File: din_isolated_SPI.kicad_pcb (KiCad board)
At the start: 2 copper layers, 31.8 x 40.5 mm, 19 parts, among them J1 CONN_01X10, U1 SI8661AB-B-IS1, U4 WeMos_mini

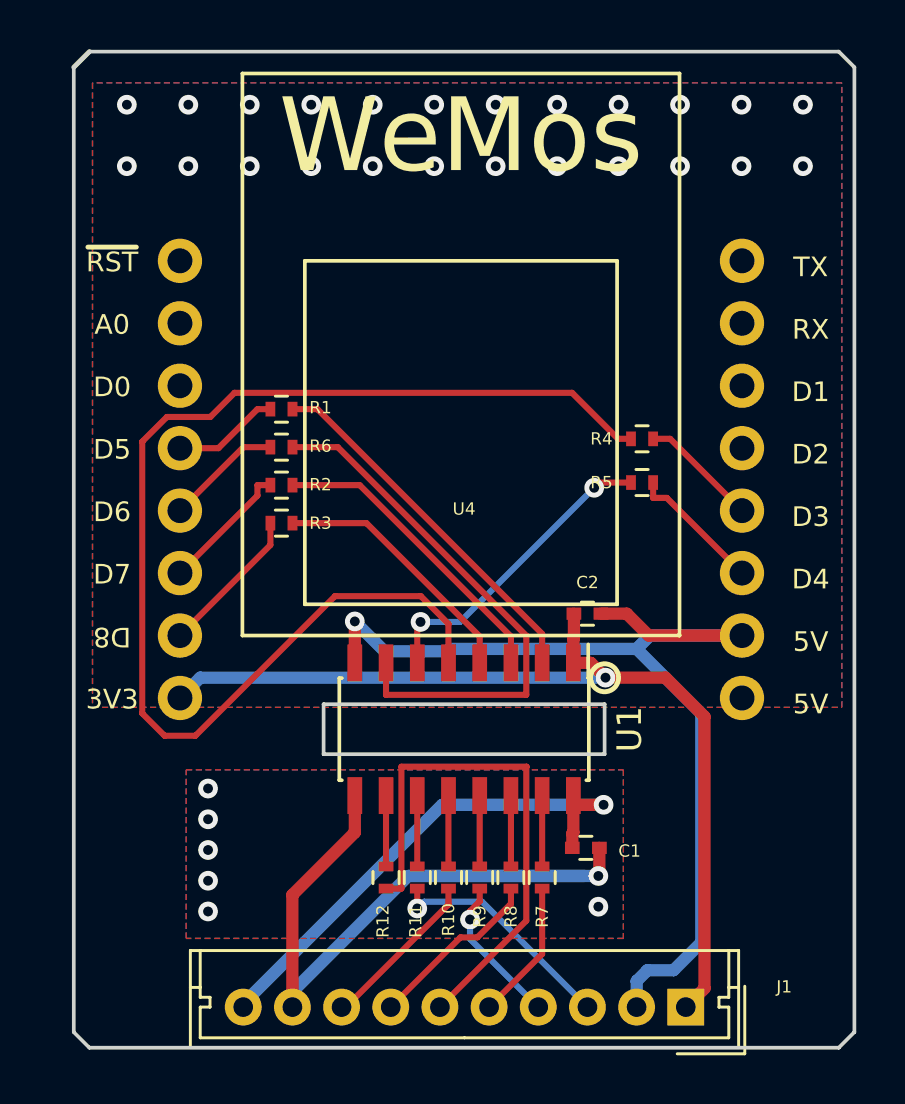
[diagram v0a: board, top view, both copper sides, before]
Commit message: Change to 0603 and reroute
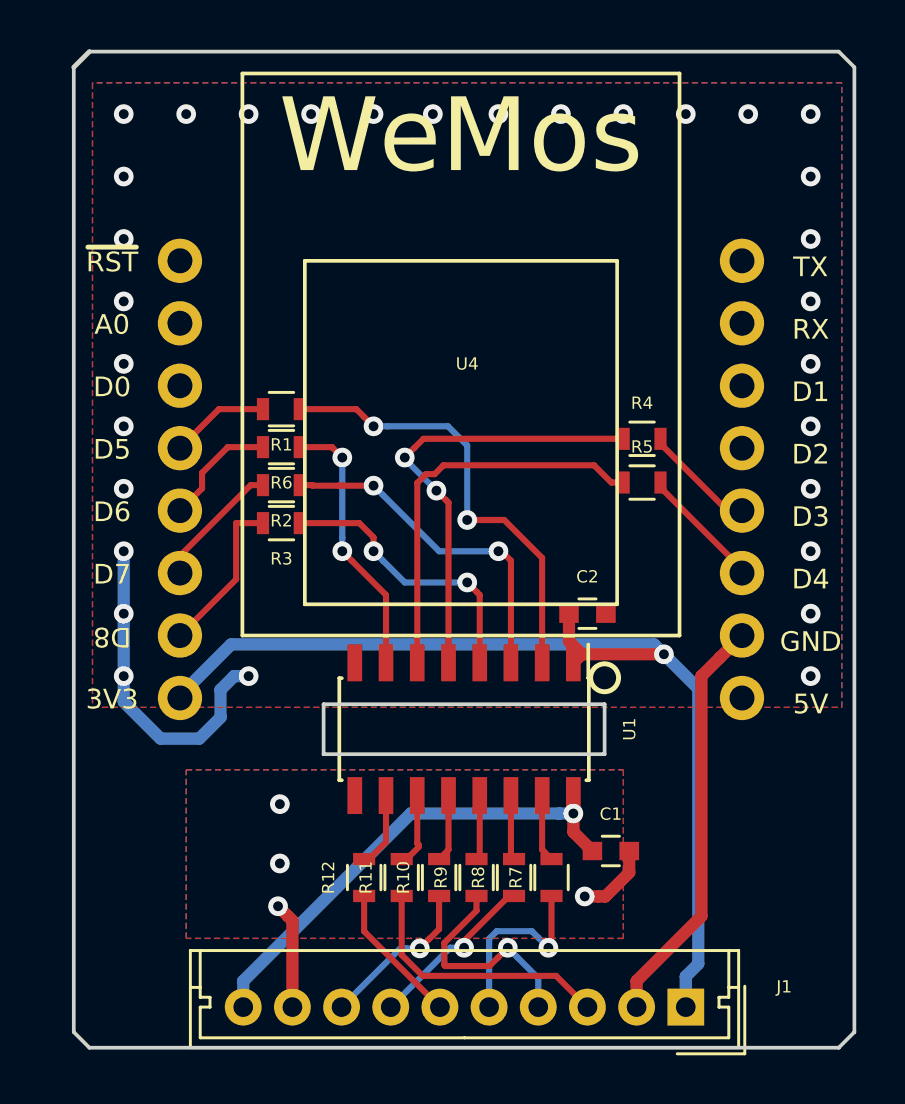
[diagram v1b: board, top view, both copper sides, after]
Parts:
- C1, C2: footprint Capacitors_SMD:C_0402 -> Capacitors_SMD:C_0603
- R1, R10, R11, R12, R2, R3, R4, R5, R6, R7, R8, R9: footprint Resistors_SMD:R_0402 -> Resistors_SMD:R_0603
- moved C1 1.02 mm to (138.7, 83.4)
- moved R12 0.89 mm to (128.7, 84.5)
- moved R11 0.63 mm to (130.2, 84.5)
- moved R10 0.38 mm to (131.7, 84.5)
- moved R7 0.38 mm to (136.3, 84.5)
- moved R8 0.13 mm to (134.7, 84.5)
- moved R9 0.13 mm to (133.2, 84.5)
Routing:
- net Net-(R4-Pad1): track 49.8 -> 18.3 mm, vias 0 -> 2
- net GND_I: track 33.0 -> 7.44 mm, vias 7 -> 4
- net MISO_E: track 21.9 -> 5.80 mm
- net GND_C: track 41.7 -> 30.4 mm, vias 25 -> 31
- net Net-(R6-Pad1): track 22.1 -> 11.0 mm, vias 0 -> 2
- net Net-(R5-Pad1): track 12.6 -> 16.3 mm, vias 2 -> 0
- net 3V3_C: track 38.0 -> 41.6 mm
- net Net-(R1-Pad1): track 15.1 -> 18.4 mm, vias 0 -> 2
- net CS0_E: track 6.13 -> 9.18 mm
- net CLK_E: track 5.71 -> 7.76 mm, vias 0 -> 1
- net Net-(R2-Pad1): track 12.5 -> 14.2 mm, vias 0 -> 2
- net 3V3_I: track 21.5 -> 20.0 mm
- net CS2_E: track 9.62 -> 10.8 mm, vias 1 -> 0
- net Net-(R3-Pad1): track 10.6 -> 11.7 mm, vias 0 -> 2
- net CS0_W: track 6.10 -> 6.61 mm
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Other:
- board text added: "TAPR"
- board text added: "Wemos Isolated SPI Basic v1.2 23/12/2017"
- board text removed: "Wemos Isolated SPI Basic v1.1 22/11/2017"
